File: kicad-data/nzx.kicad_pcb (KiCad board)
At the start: 2 copper layers, 271.5 x 184.5 mm, 27 parts

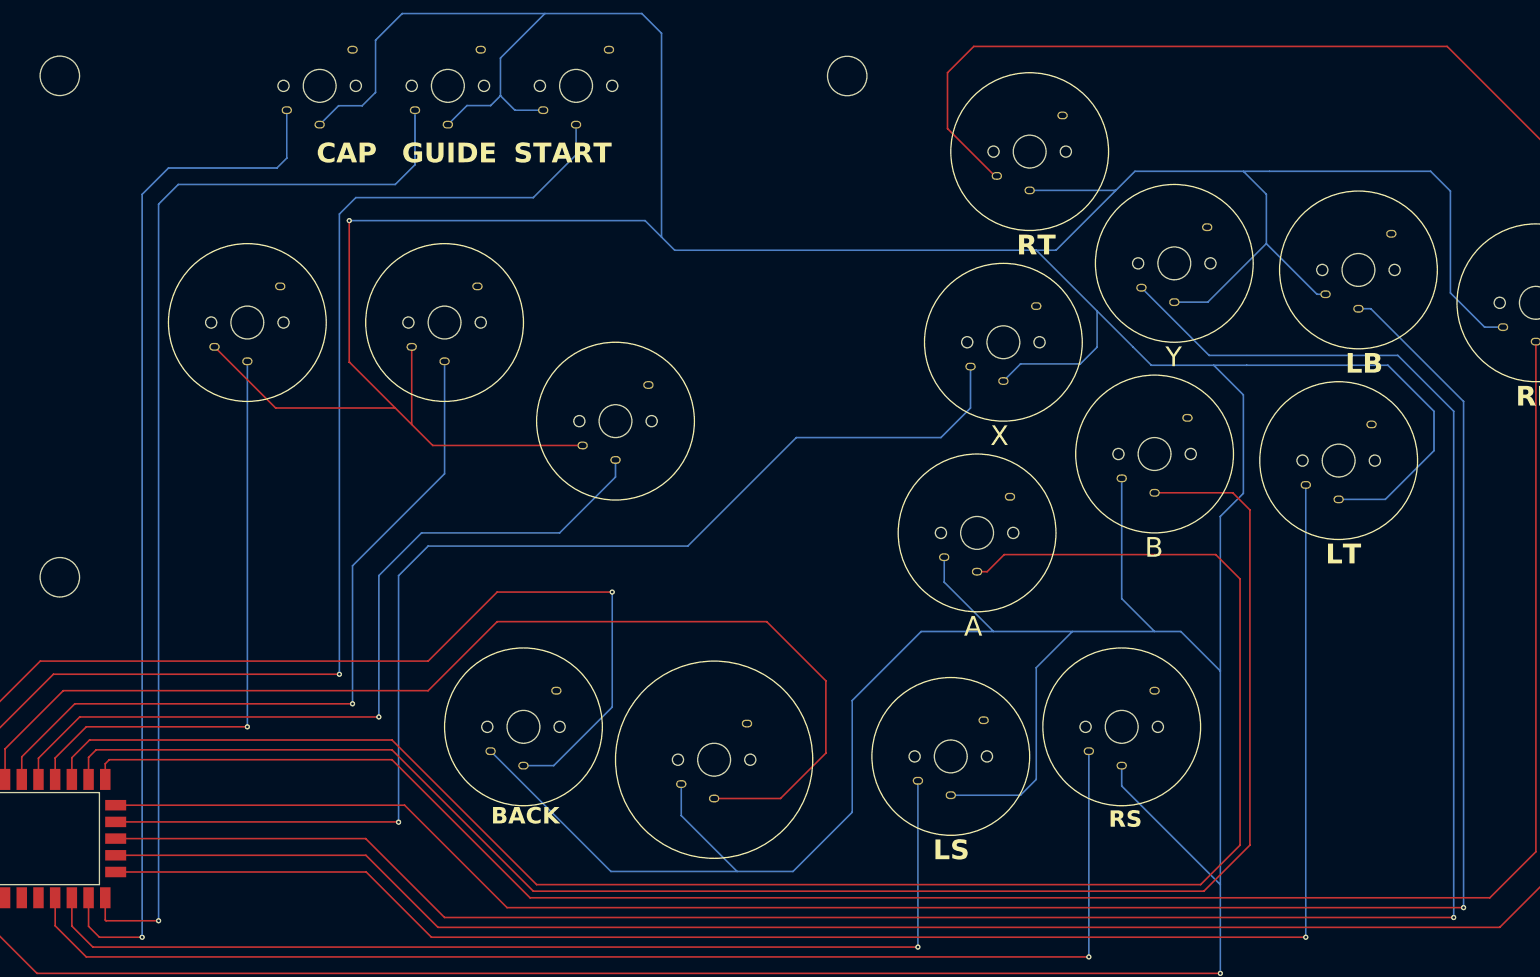
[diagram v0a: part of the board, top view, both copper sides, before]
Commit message: fix: Update button wiring and adjust edge data
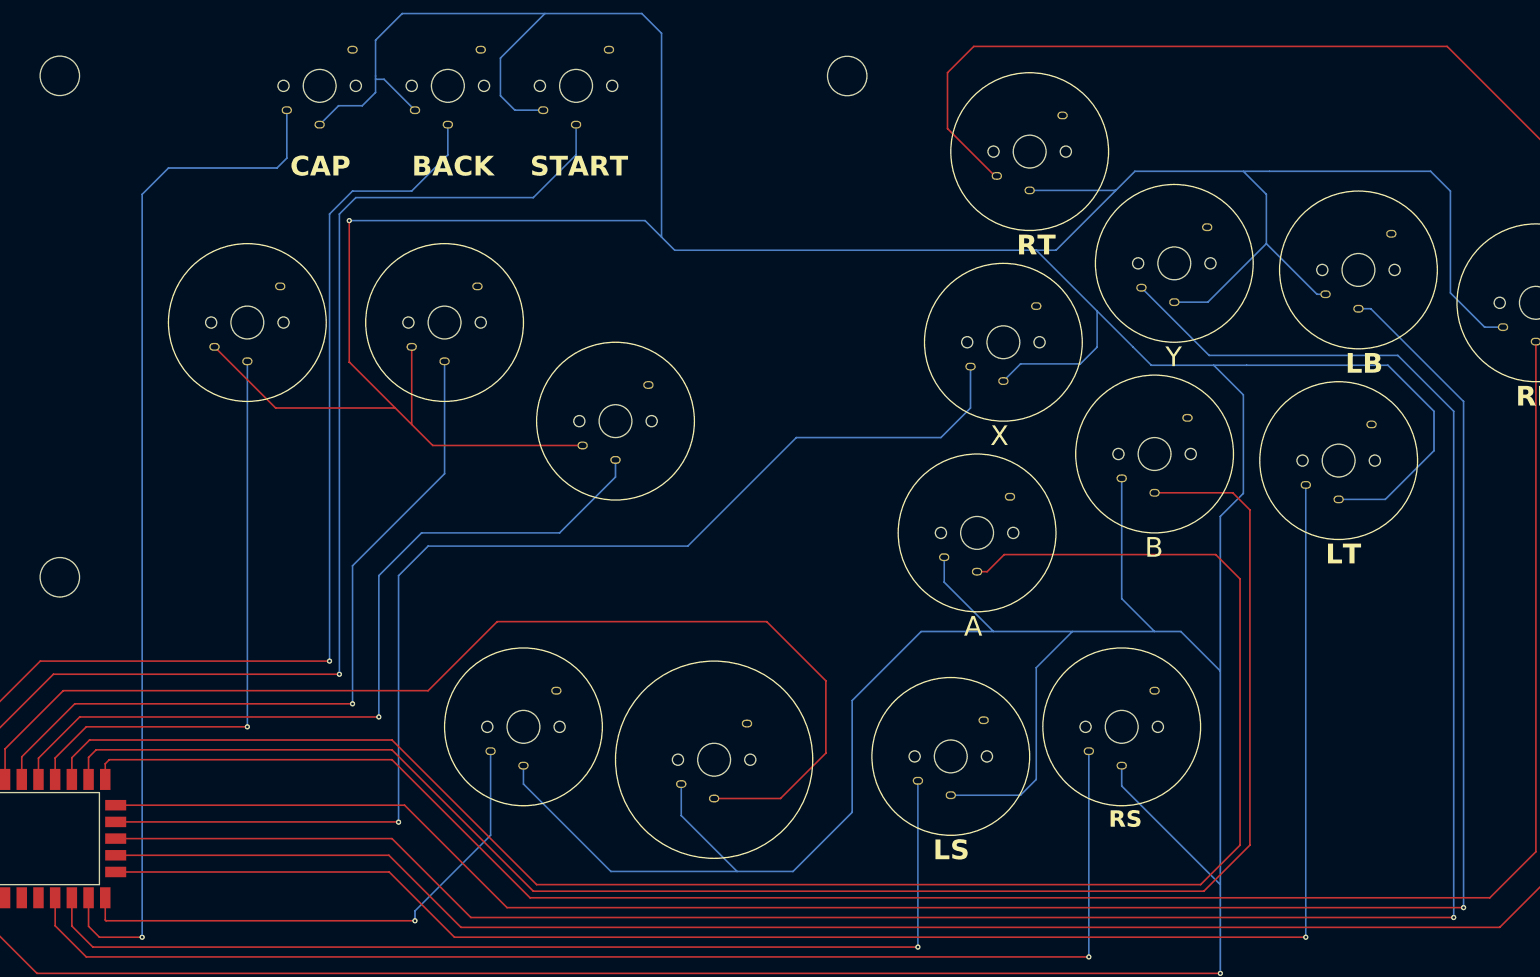
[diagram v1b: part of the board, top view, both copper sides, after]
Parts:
- A1(GUIDE)1: footprint Kailh_Choc_V2:Kailh_Choc_V2 -> Kailh_Choc_V2:Kailh_Choc_V2_24
- S1(BACK)1: footprint Kailh_Choc_V2:Kailh_Choc_V2_24 -> Kailh_Choc_V2:Kailh_Choc_V2
- moved A1(GUIDE)1 98.2 mm to (86.5, 115.0)
- moved S1(BACK)1 98.2 mm to (75.0, 17.5)
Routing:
- net Net-(RZ1-GP14): track 170.3 -> 81.1 mm
- net Net-(RZ1-GP0): track 148.4 -> 160.7 mm
- net Net-(RZ1-GND): track 1163.3 -> 1157.2 mm
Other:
- board text removed: "GUIDE"
